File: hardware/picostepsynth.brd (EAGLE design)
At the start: 177.8 x 81.3 mm, 57 parts, among them J1 AUDIO-JACK-TRRS, J2 AUDIO-JACK-TRRS, P1 10k, P2 10k, P3 10k, P4 10k, P5 10k, P6 10k, P7 10k, P8 10k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

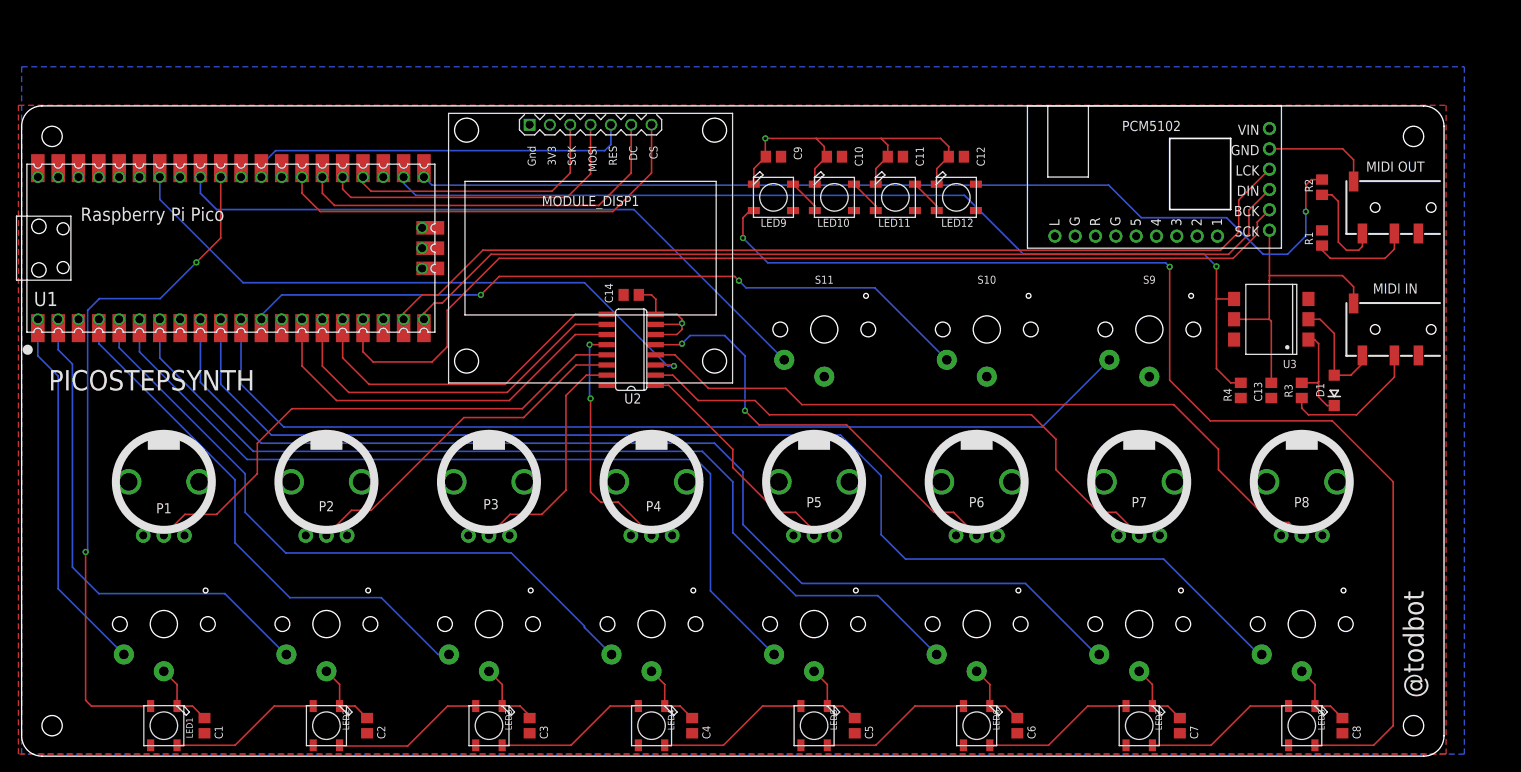
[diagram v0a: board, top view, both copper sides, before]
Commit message: brd: make larger to support a proper case
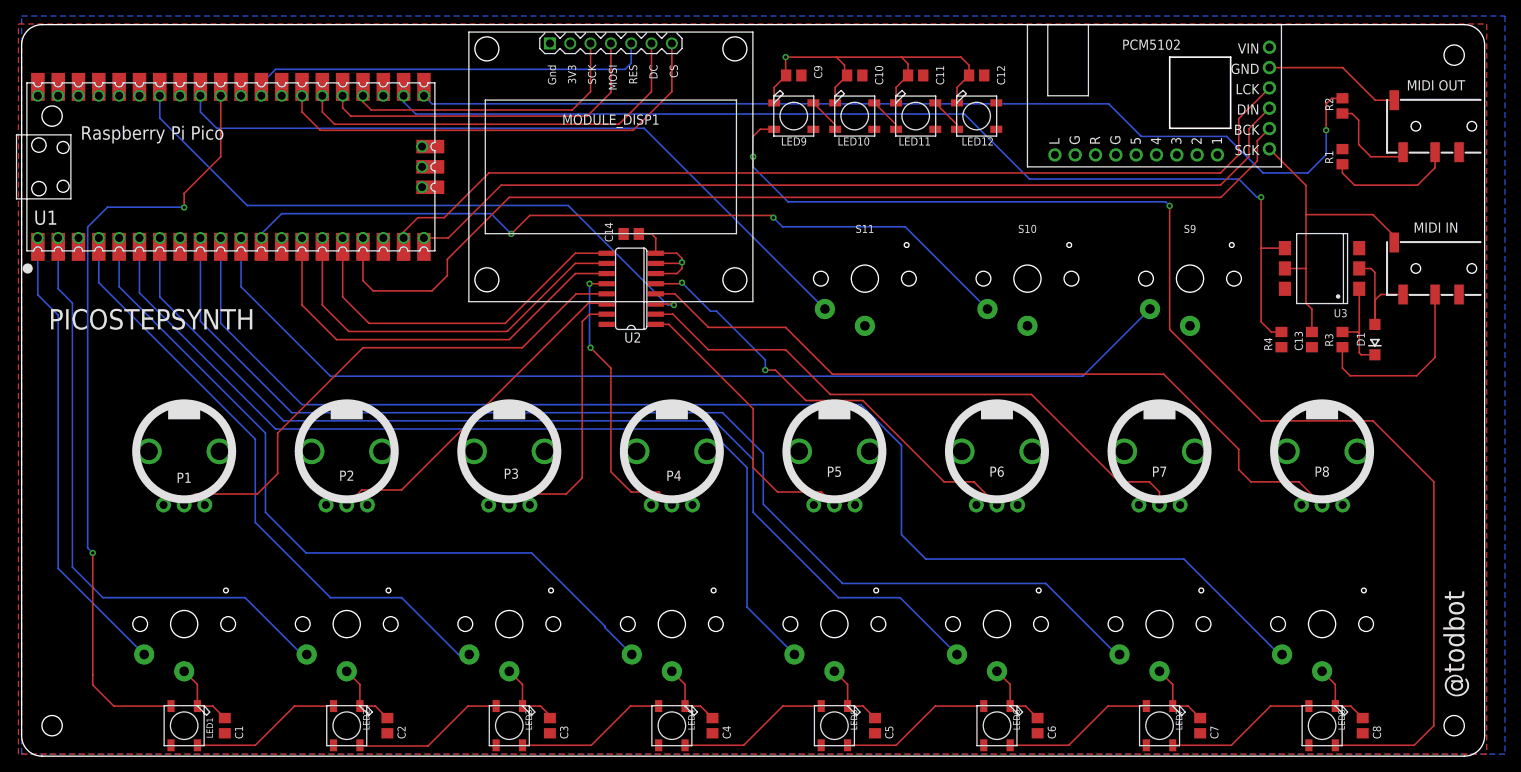
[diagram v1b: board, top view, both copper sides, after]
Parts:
- moved J1 11.4 mm to (182.9, 78.7)
- moved LED10 10.5 mm to (104.1, 80.0)
- moved LED11 10.5 mm to (111.8, 80.0)
- moved LED12 10.5 mm to (119.4, 80.0)
- moved LED9 10.5 mm to (96.5, 80.0)
- moved R1 10.5 mm to (165.1, 74.9)
- moved C10 10.5 mm to (104.1, 85.1)
- moved C11 10.5 mm to (111.8, 85.1)
- moved C12 10.5 mm to (119.4, 85.1)
- moved C9 10.5 mm to (96.5, 85.1)
- moved MODULE_DISP1 10.5 mm to (73.7, 73.7)
- moved R2 10.5 mm to (165.1, 81.3)
- moved MODULE_PCM5102A 10.2 mm to (157.5, 73.7)
- moved U1 10.2 mm to (26.2, 73.7)
- moved J2 9.16 mm to (182.9, 61.0)
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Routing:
- net N$17: track 147.8 -> 161.1 mm
- net SW2: track 64.1 -> 76.8 mm
- net NEOPIXEL: track 86.4 -> 98.5 mm
- net SW4: track 85.0 -> 96.2 mm
- net SW1: track 47.5 -> 58.7 mm
- net SW8: track 157.7 -> 168.1 mm
- net SW5: track 108.8 -> 118.8 mm
- net SW3: track 68.6 -> 78.4 mm
- net MIDI_IN: track 126.5 -> 135.6 mm
- net SW6: track 122.1 -> 130.5 mm
- net SW7: track 139.3 -> 147.4 mm
- net GND: track 197.3 -> 204.7 mm
- net POT5: track 29.3 -> 36.0 mm
- net SW10: track 93.6 -> 100.3 mm
- net SW11: track 84.7 -> 91.4 mm
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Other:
- board size 177.8 x 81.3 mm -> 182.9 x 91.4 mm
